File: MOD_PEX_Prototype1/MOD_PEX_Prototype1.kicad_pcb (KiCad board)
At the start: 2 copper layers, 78.4 x 40 mm, 66 parts, among them CN1 CONN_PANNEL_2X2, CN2 CONN_PANNEL_2X2, J1 RJ45_CHAIN, J2 RJ45_CHAIN, P1 HEADER_3X1, P2 HEADER_5X1, P3 HEADER_5X2, P4 HEADER_2X1, Q1 MMBT3904, Q2 MMBT3904, SW1 SWITCH_HH, U1 LPC111X_LQFP48, U2 AP1117E50G, U3 AP1117E33G, U4 SN75176BDR, X1 10MHz

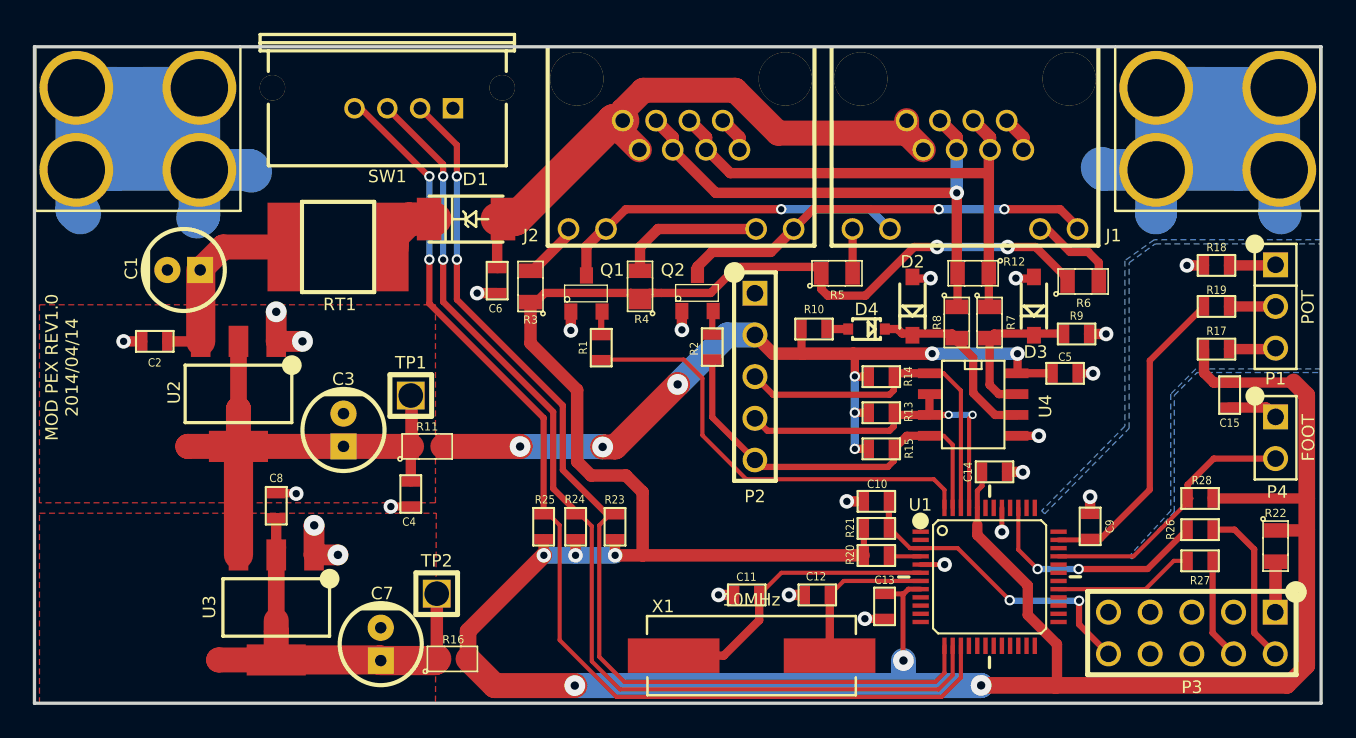
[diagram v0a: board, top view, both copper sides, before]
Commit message: fix issue #7: protect the U4 IC when the board is being debugged updated the pcb traces and Gerber outputs.
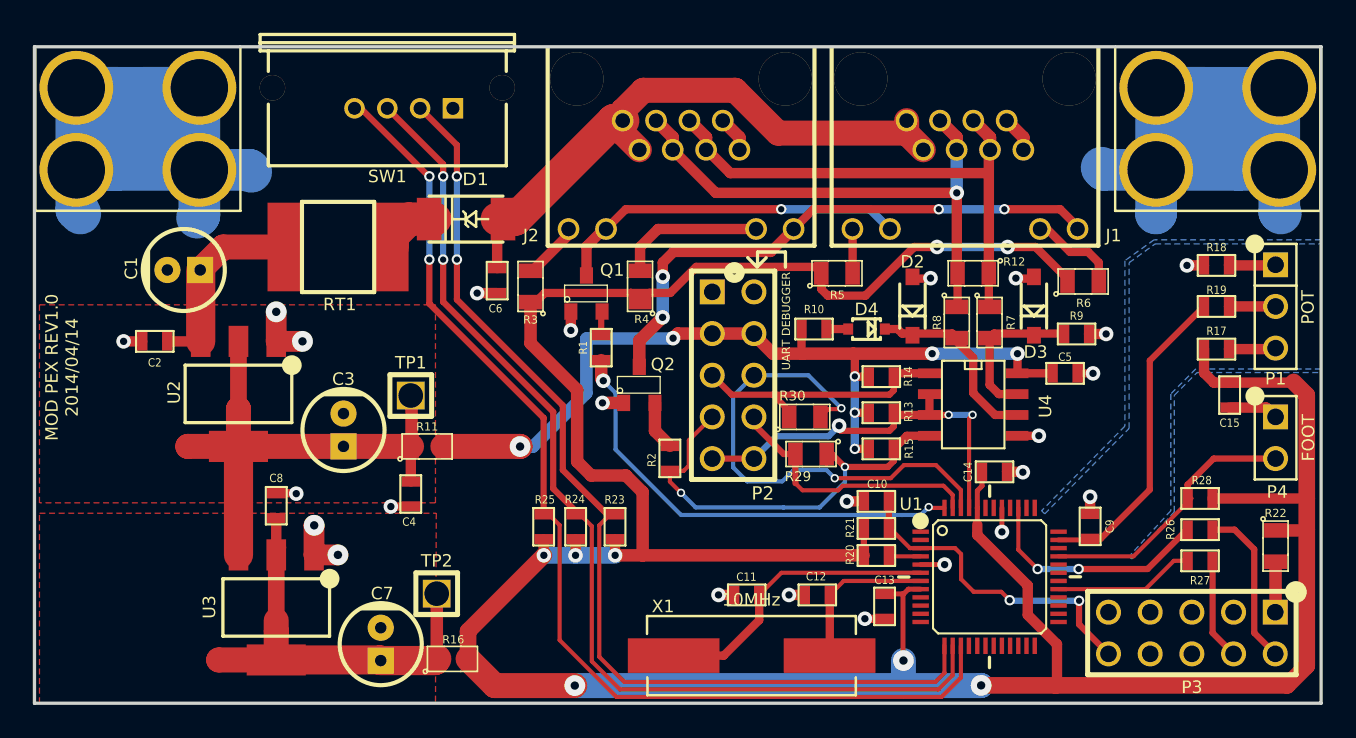
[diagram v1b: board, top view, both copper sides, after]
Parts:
- added R29: 0R, MOD_Footprints_Lib:SM0805, F.Cu at (110.8, 88.3)
- added R30: 0R, MOD_Footprints_Lib:SM0805, F.Cu at (110.4, 86.1)
- P2: value HEADER_5X1 -> HEADER_5X2; footprint MOD_Footprints_Lib:PIN_ARRAY_5x1 -> MOD_Footprints_Lib:PIN_ARRAY_5x2
- moved R2 7.26 mm to (102.2, 88.6)
- moved Q2 6.63 mm to (100.4, 84.1)
- moved P2 1.33 mm to (106.1, 83.5)
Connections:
- P2 pad 2: +5V -> DGND
- P2 pad 3: RX_CHAIN -> +5V
- P2 pad 4: EN_CHAIN -> +5V
- P2 pad 5: TX_CHAIN -> RX_CHAIN
- U1 pad 46: RX_CHAIN -> Net-(P2-Pad6)
- U1 pad 47: TX_CHAIN -> Net-(P2-Pad8)
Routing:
- net Net-(P2-Pad6): track 0.00 -> 30.6 mm, vias 0 -> 2
- net Net-(P2-Pad8): track 0.00 -> 16.4 mm
- net Net-(J1-Pad12): track 25.7 -> 34.4 mm, vias 2 -> 4
- net RX_CHAIN: track 21.6 -> 16.5 mm
- net EN_CHAIN: track 21.6 -> 25.0 mm, vias 2 -> 3
- net TX_CHAIN: track 24.7 -> 26.8 mm, vias 0 -> 2
- net +5V: track 51.9 -> 53.8 mm, vias 8 -> 7
- net Net-(Q2-Pad2): track 1.46 -> 3.00 mm
- net RESET: track 19.0 -> 19.9 mm
- net LED1: track 27.4 -> 27.8 mm, vias 0 -> 2
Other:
- board text added: "UART DEBUGGER"

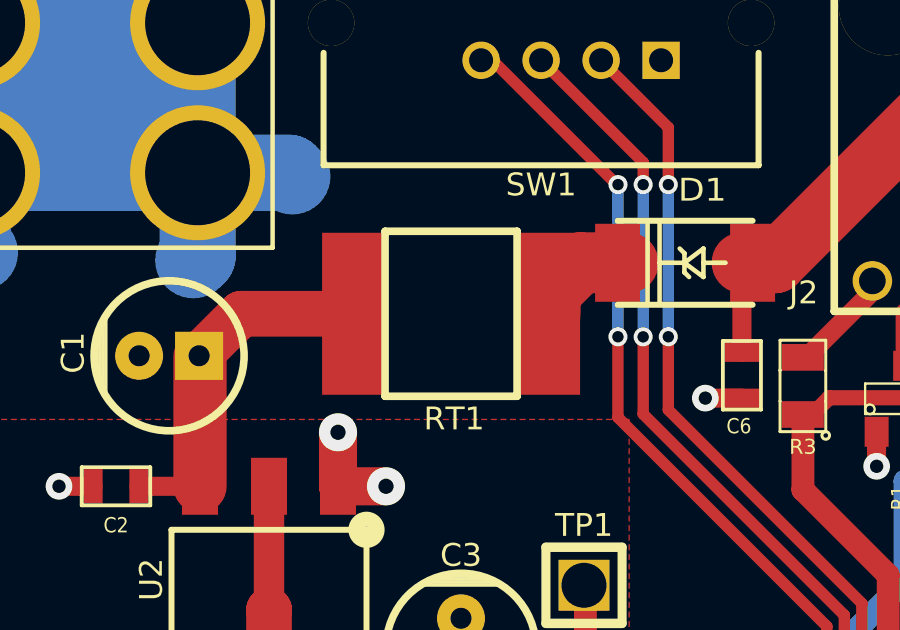
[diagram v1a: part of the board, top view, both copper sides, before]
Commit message: fix issue #9: change footprint of RT1 (updated pcb traces and gerber outputs)
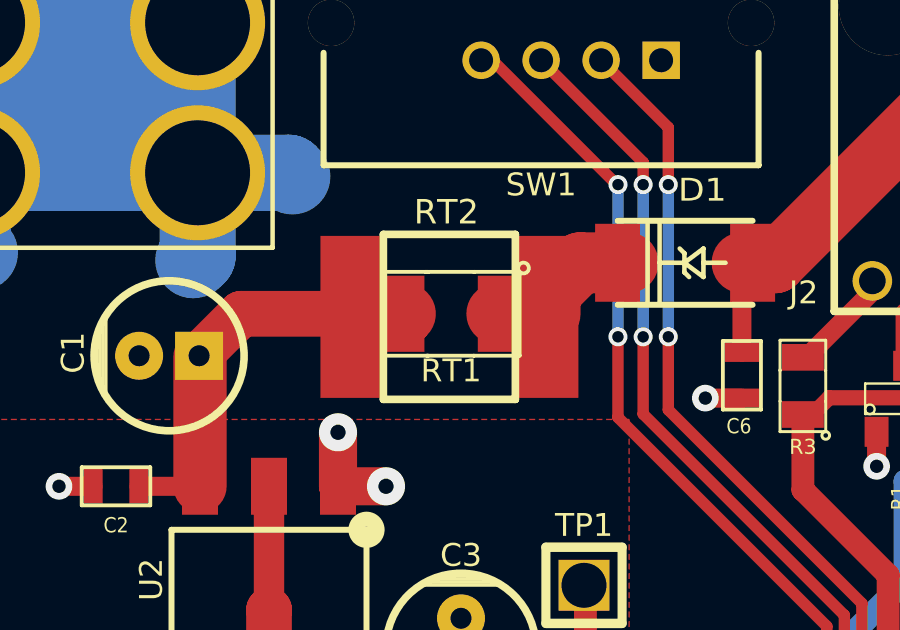
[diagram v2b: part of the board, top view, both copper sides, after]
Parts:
- added RT2: PTC_FUSE, MOD_Footprints_Lib:SM2920, F.Cu at (81.9, 75.8)
- RT1: footprint MOD_Footprints_Lib:SM2920 -> MOD_Footprints_Lib:SM1210
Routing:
- net +9V: track 12.2 -> 14.1 mm
- net Net-(D1-Pad2): track 3.71 -> 5.48 mm

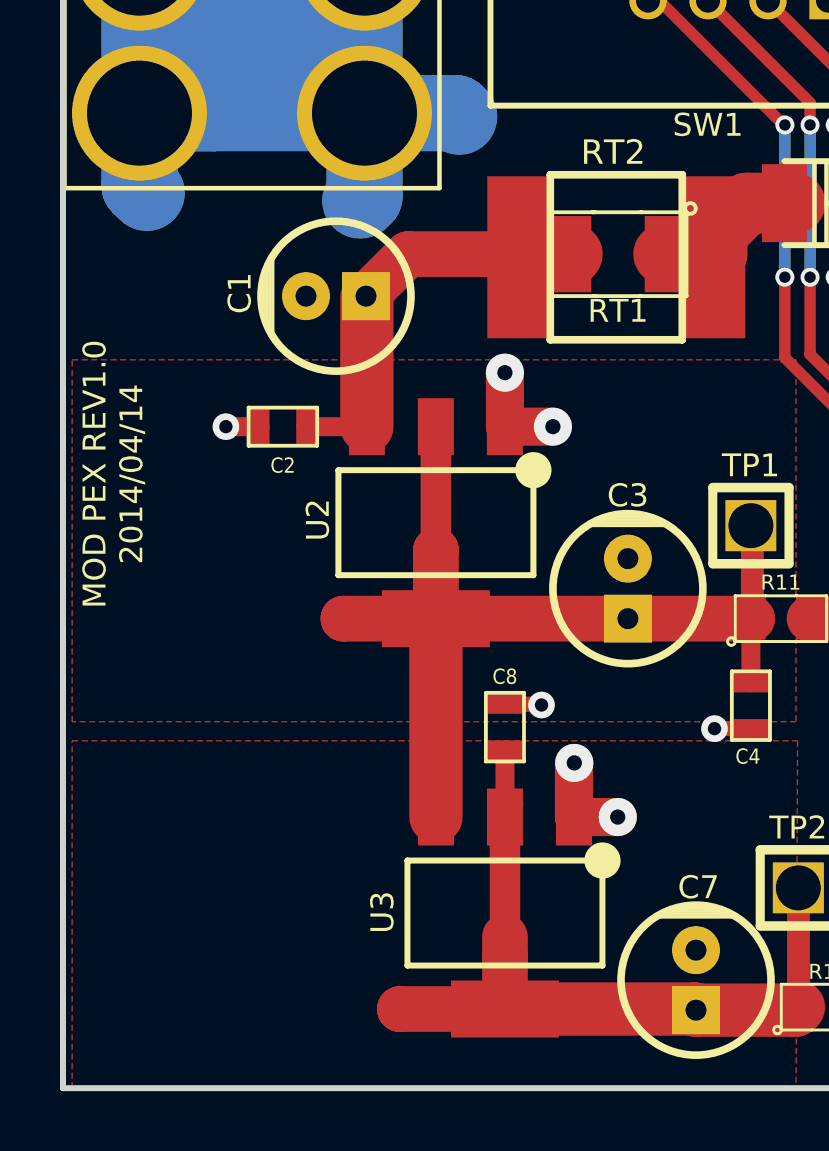
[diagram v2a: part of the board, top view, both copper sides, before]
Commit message: fix issue #3: Add "CC by-SA" license logo to the PCB silk layer I have adapted and rearranged the previous silk text as well.
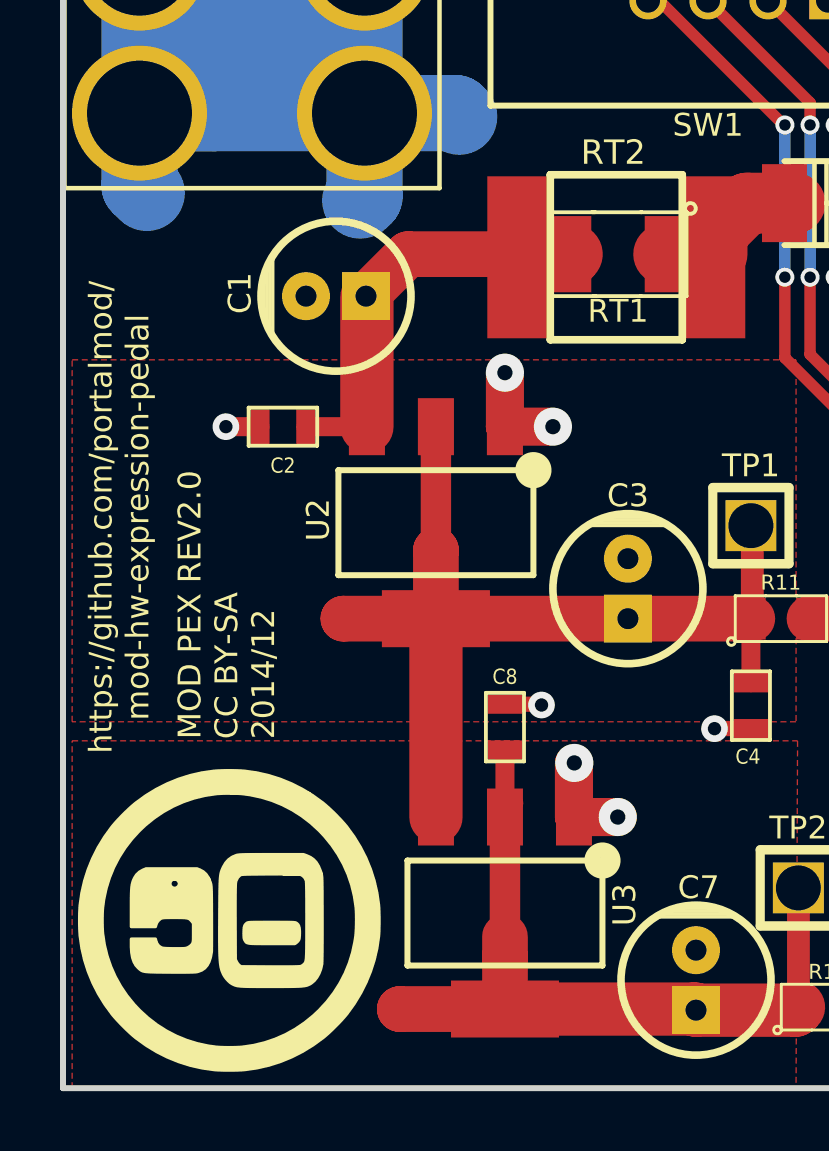
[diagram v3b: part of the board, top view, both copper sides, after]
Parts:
- added LOGO: LOGO, MOD_Footprints_Lib:MOD_Logo, F.Cu at (69.0, 97.9)
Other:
- board text added: "MOD PEX REV2.0 CC BY-SA 2014/12"
- board text added: "https://github.com/portalmod/ mod-hw-expression-pedal"
- board text removed: "MOD PEX REV1.0 2014/04/14"

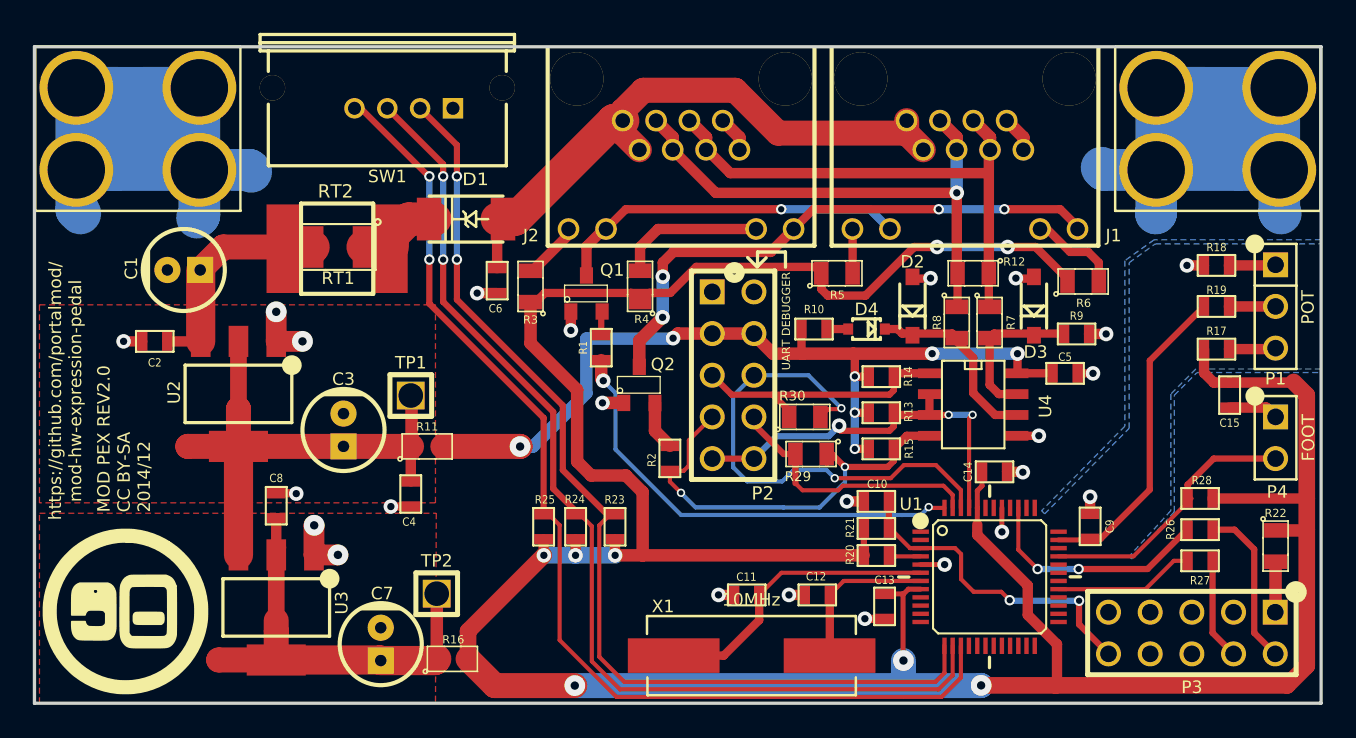
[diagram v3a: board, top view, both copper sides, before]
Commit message: wip issue #11: tracing the PCB signals
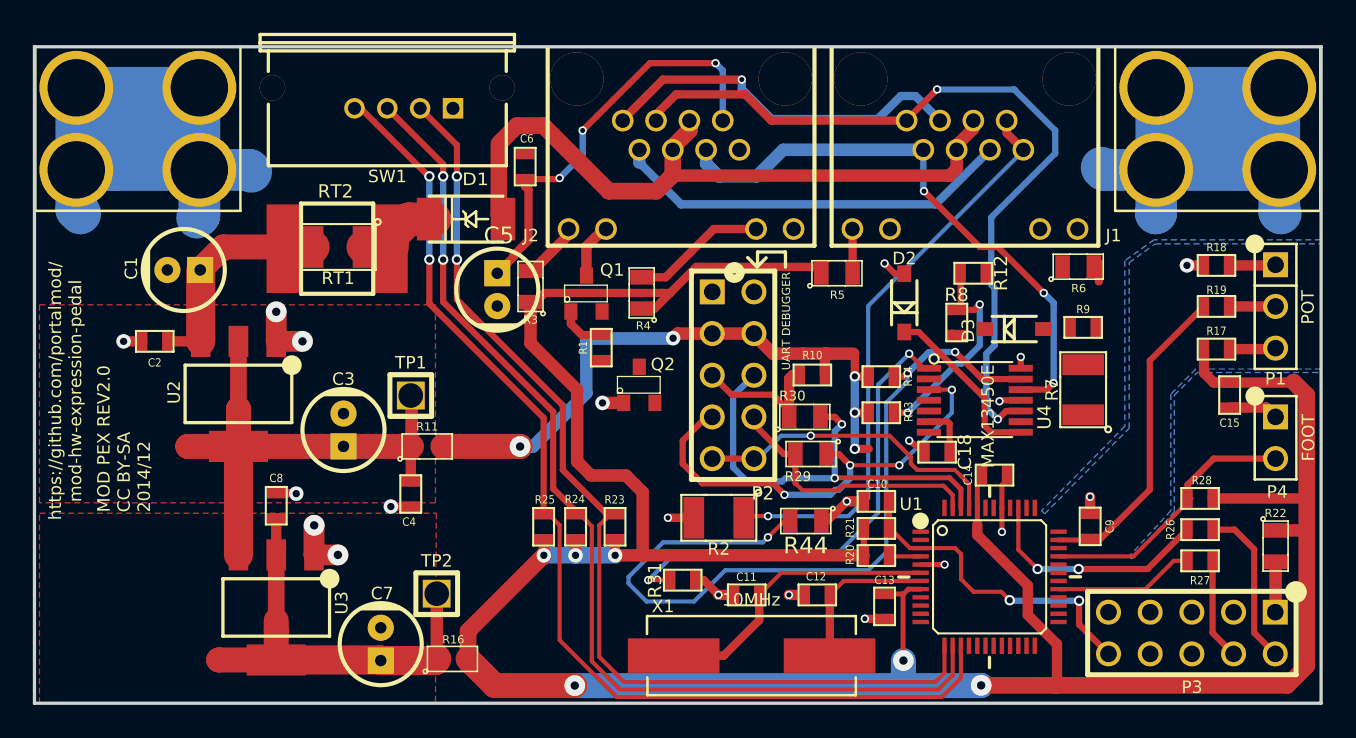
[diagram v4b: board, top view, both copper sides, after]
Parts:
- removed D4: 1N4148, MOD_Footprints_Lib:SOD323
- removed LOGO: LOGO, MOD_Footprints_Lib:MOD_Logo
- removed R15: 10k, MOD_Footprints_Lib:SM0603
- added C18: 100nF_X7R, MOD_Footprints_Lib:SM0603, F.Cu at (118.5, 88.2)
- added R31: 10k, MOD_Footprints_Lib:SM0603, F.Cu at (103.0, 96.0)
- added R44: 0R/NC, MOD_Footprints_Lib:SM0805, F.Cu at (110.5, 92.4)
- C5: value 100nF_X7R -> 100uF; footprint MOD_Footprints_Lib:SM0603 -> MOD_Footprints_Lib:CAP_RAD_5MM
- J1: value RJ45_CHAIN -> RJ45_CHAIN_MAIN
- J2: value RJ45_CHAIN -> RJ45_CHAIN_EXTENSION
- Q2: value MMBT3904 -> MMBT3906
- R10, R9: value 1k -> 10k
- R12: value 120R -> 10k; footprint MOD_Footprints_Lib:SM0805 -> MOD_Footprints_Lib:SM0603
- R2: value 1k -> 100R 0.5W; footprint MOD_Footprints_Lib:SM0603 -> MOD_Footprints_Lib:SM1210
- R7: value 10R -> 100R 0.5W; footprint MOD_Footprints_Lib:SM0805 -> MOD_Footprints_Lib:SM1210
- R8: value 10R -> 1k; footprint MOD_Footprints_Lib:SM0805 -> MOD_Footprints_Lib:SM0603
- U4: value SN75176BDR -> MAX13450E; footprint MOD_Footprints_Lib:SO8E -> MOD_Footprints_Lib:TSSOP14
- moved C5 35.0 mm to (91.7, 78.3)
- moved C6 7.16 mm to (93.4, 70.8), turned to 90 degrees
- moved R7 7.02 mm to (127.4, 84.4), turned to 90 degrees
- moved R2 4.69 mm to (105.2, 92.2), turned to 180 degrees
- moved R10 2.80 mm to (110.9, 83.5)
- moved D3 1.84 mm to (123.2, 80.7), turned to 0 degrees
- moved R6 0.95 mm to (127.1, 76.9)
- moved R9 0.57 mm to (127.4, 80.6)
- moved D2 0.54 mm to (116.5, 79.1)
- moved R4 0.41 mm to (100.5, 78.5)
- moved U4 0.32 mm to (120.8, 85.0)
- moved C14 0.20 mm to (122.0, 89.6)
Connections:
- C5 pad 1: +5V -> Net-(C5-Pad1)
- C6 pad 1: VCC -> Net-(C5-Pad1)
- D2 pad 2: Net-(D2-Pad2) -> RS485_RX+
- D3 pad 2: Net-(D3-Pad2) -> RS485_RX-
- J1 pad 1: VCC -> RS485_TX+
- J1 pad 12: Net-(J1-Pad12) -> DGND
- J1 pad 2: VCC -> RS485_TX-
- J1 pad 3: RS422_A -> RS485_RX+
- J1 pad 4: RS422_A -> VCC
- J1 pad 5: RS422_B -> VCC
- J1 pad 6: RS422_B -> RS485_RX-
- J1 pad 7: DGND -> Net-(J1-Pad7)
- J1 pad 8: DGND -> Net-(J1-Pad7)
- J2 pad 1: VCC -> RS485_RX+
- J2 pad 12: Net-(J1-Pad12) -> DGND
- J2 pad 2: VCC -> RS485_RX-
- J2 pad 3: RS422_A -> RS485_TX+
- J2 pad 4: RS422_A -> VCC
- J2 pad 5: RS422_B -> VCC
- J2 pad 6: RS422_B -> RS485_TX-
- J2 pad 7: DGND -> Net-(C5-Pad1)
- J2 pad 8: DGND -> Net-(J2-Pad8)
- Q1 pad 1: DGND -> Net-(Q1-Pad1)
- Q1 pad 2: Net-(Q1-Pad2) -> DGND
- Q2 pad 1: DGND -> Net-(Q2-Pad1)
- Q2 pad 2: Net-(Q2-Pad2) -> +5V
- Q2 pad 3: Net-(J1-Pad12) -> RTERM_CHAIN
- R1 pad 1: LED1 -> LED5
- R1 pad 2: Net-(Q1-Pad2) -> Net-(Q1-Pad1)
- R10 pad 1: Net-(D4-Pad1) -> +5V
- R10 pad 2: +5V -> RX_CHAIN
- R12 pad 1: RS422_B -> Net-(C5-Pad1)
- R12 pad 2: RS422_A -> Net-(R12-Pad2)
- R13 pad 2: EN_CHAIN -> Net-(R12-Pad2)
- R14 pad 2: RX_CHAIN -> Net-(R14-Pad2)
- R2 pad 1: TX_CHAIN -> Net-(J1-Pad7)
- R2 pad 2: Net-(Q2-Pad2) -> DGND
- R7 pad 1: RS422_B -> Net-(J2-Pad8)
- R7 pad 2: Net-(D3-Pad2) -> DGND
- R8 pad 1: RS422_A -> Net-(R12-Pad2)
- R8 pad 2: Net-(D2-Pad2) -> Net-(Q2-Pad1)
- R9 pad 1: DGND -> RTERM_CHAIN
- R9 pad 2: Net-(D3-Pad2) -> DGND
- U4 pad 1: RX_CHAIN -> TX_CHAIN_EN
- U4 pad 2: EN_CHAIN -> DGND
- U4 pad 3: EN_CHAIN -> TX_CHAIN
- U4 pad 4: TX_CHAIN -> +5V
- U4 pad 5: DGND -> RTERM_CHAIN
- U4 pad 6: Net-(D2-Pad2) -> Net-(C18-Pad1)
- U4 pad 7: Net-(D3-Pad2) -> RX_CHAIN
- U4 pad 8: +5V -> RS485_RX+
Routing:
- net Net-(R14-Pad2): track 0.00 -> 49.8 mm, vias 0 -> 3
- net RS485_TX+: track 0.00 -> 49.1 mm, vias 0 -> 2
- net RS485_TX-: track 0.00 -> 35.5 mm, vias 0 -> 3
- net Net-(J1-Pad7): track 0.00 -> 35.4 mm, vias 0 -> 1
- net Net-(J1-Pad12): track 34.4 -> 0.00 mm, vias 4 -> 0
- net RS485_RX+: track 0.00 -> 33.6 mm, vias 0 -> 1
- net RS422_A: track 32.5 -> 0.00 mm, vias 1 -> 0
- net RS422_B: track 31.8 -> 0.00 mm
- net TX_CHAIN_EN: track 0.00 -> 29.1 mm, vias 0 -> 2
- net LED1: track 27.8 -> 0.00 mm, vias 2 -> 0
- net Net-(C5-Pad1): track 0.00 -> 25.7 mm, vias 0 -> 3
- net RS485_RX-: track 0.00 -> 24.7 mm
- net +3.3V: track 198.9 -> 180.3 mm, vias 8 -> 6
- net Net-(J1-Pad10): track 21.7 -> 3.43 mm, vias 1 -> 0
- net +5V: track 53.8 -> 40.1 mm, vias 7 -> 5
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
